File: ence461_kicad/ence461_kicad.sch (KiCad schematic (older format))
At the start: 52 parts

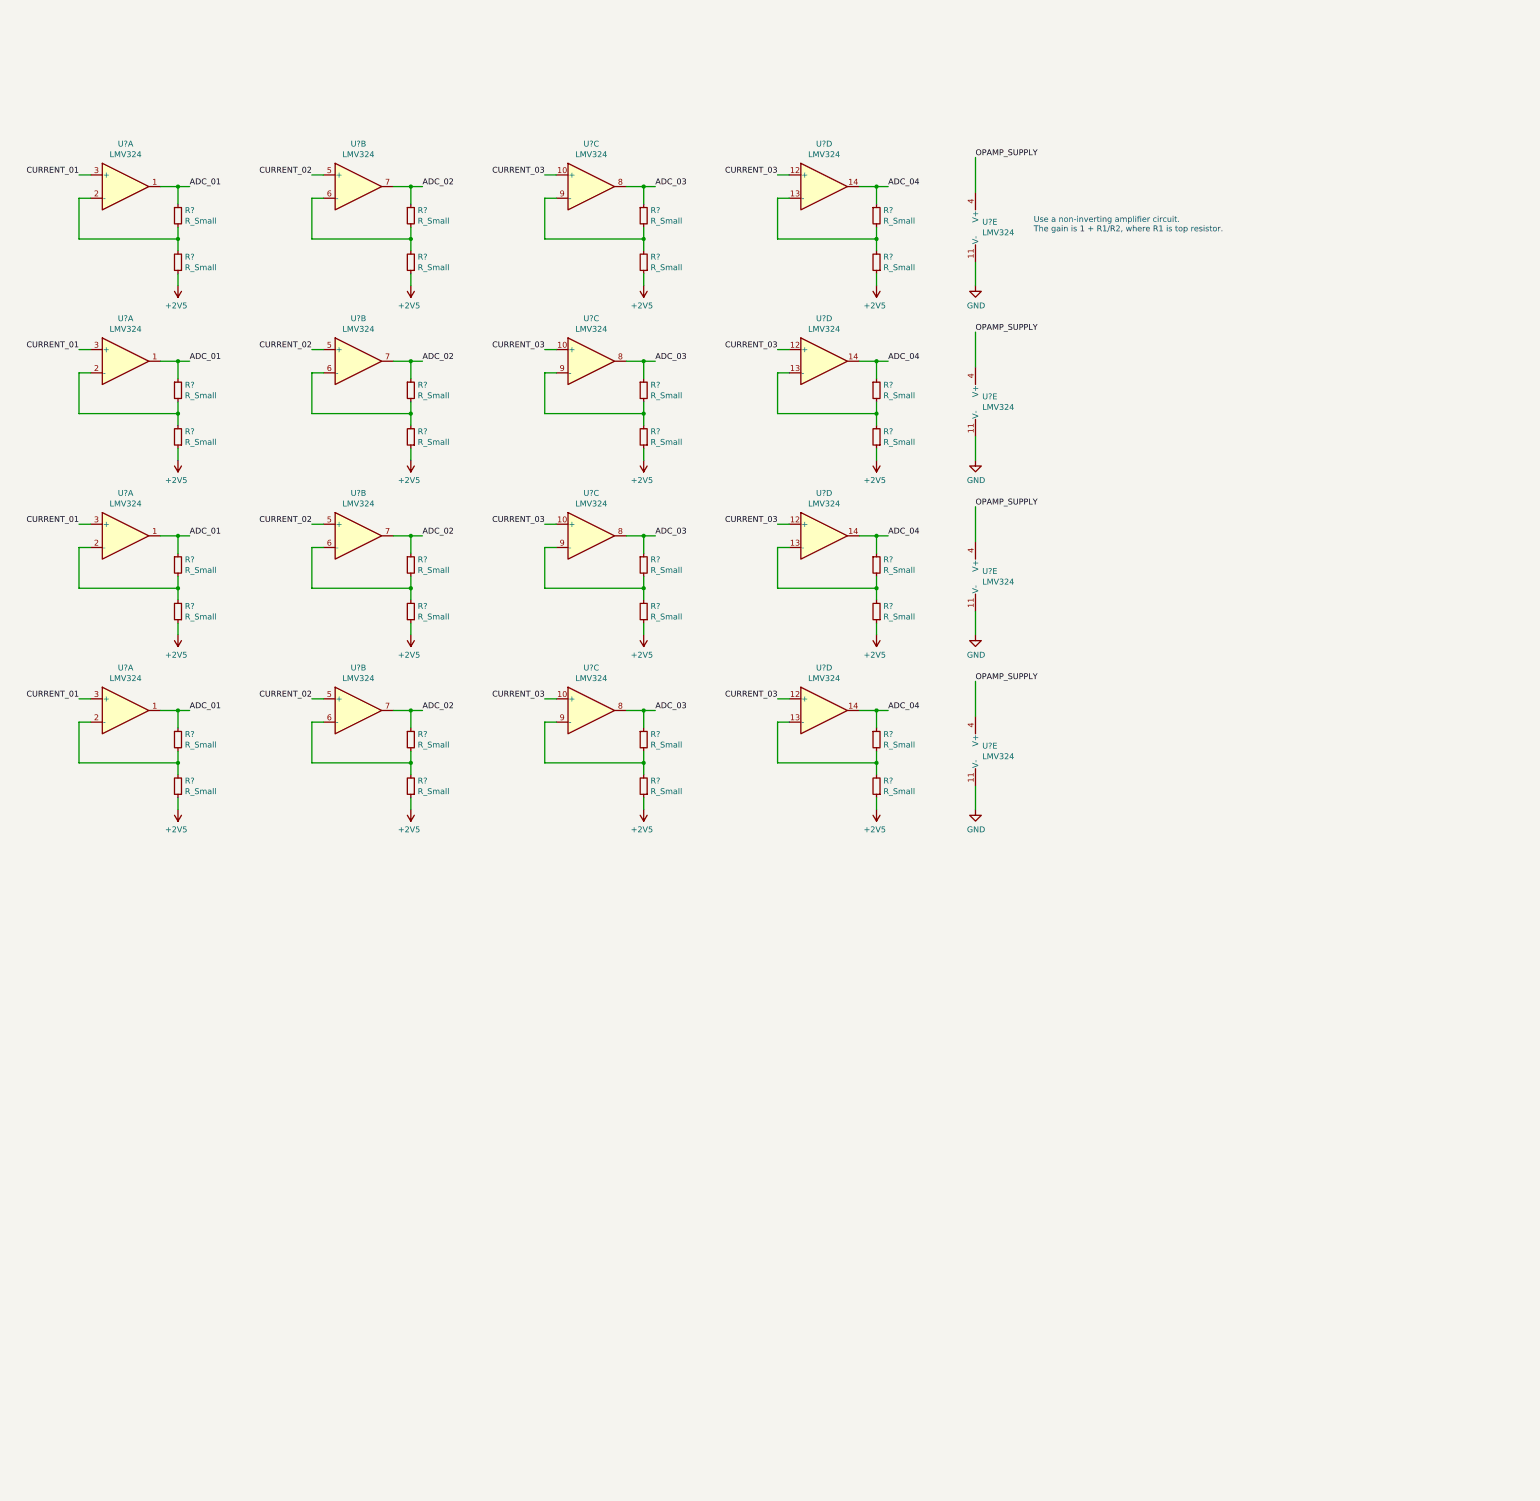
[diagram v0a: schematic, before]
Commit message: Added op amps to schematic. Specced an opamp for virtual gnd.
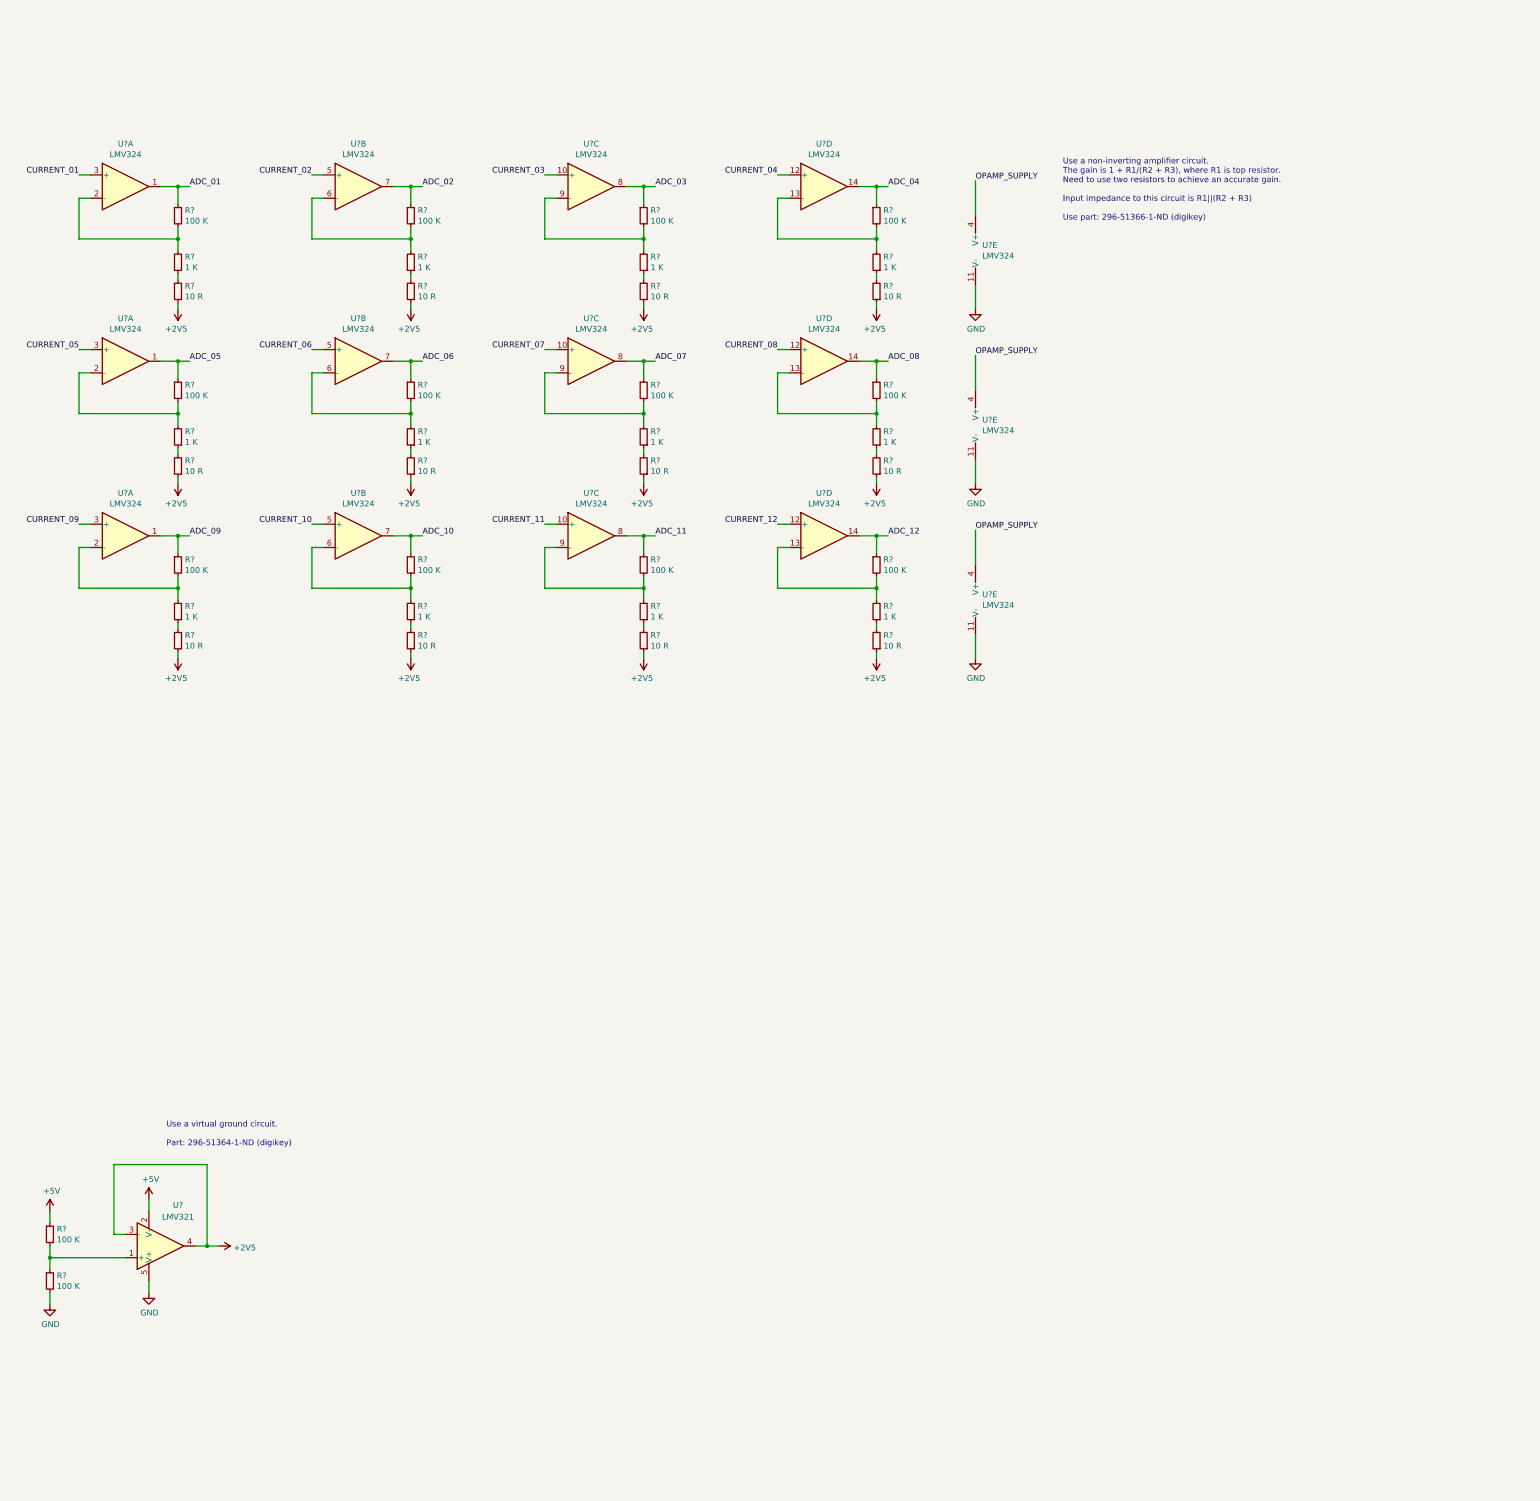
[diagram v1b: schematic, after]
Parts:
- removed R? (x24): R_Small, symbol Device:R_Small
- removed U? (x15): LMV324, symbol Amplifier_Operational:LMV324
- added R? (x12): 10 R, symbol Device:R_Small
- added R? (x10): 100 K, symbol Device:R_Small
- added R? (x8): 1 K, symbol Device:R_Small
- added U?: LMV321, symbol Amplifier_Operational:LMV321
- added U? (x10): LMV324, symbol Amplifier_Operational:LMV324
- R? (x4): value R_Small -> 100 K
- R? (x4): value R_Small -> 1 K
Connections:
- net +2V5: now also R?.1, R?.1, R?.1, R?.1, R?.1, R?.1, R?.1, R?.1, R?.1, R?.1, R?.1, R?.1, U?.3 (-), U?.4; no longer R?.1, R?.1, R?.1, R?.1
- net CURRENT_03: no longer U?.12 (+)
- net GND: now also R?.2, U?.11 (V-), U?.11 (V-), U?.5 (V+)
- net OPAMP_SUPPLY: now also U?.4 (V+), U?.4 (V+)
- new net: R?.1, R?.2 (x12)
- new net: R?.1, R?.2, U?.1 (+)
- new net: R?.2, R?.2, U?.2 (-) (x2)
- new net: R?.2, R?.2, U?.6 (-) (x2)
- new net: R?.2, R?.2, U?.9 (-) (x2)
- new net: R?.2, R?.2, U?.13 (-) (x2)
- new net +5V: R?.1, U?.2 (V-)
- new net ADC_05: R?.1, U?.1
- new net ADC_06: R?.1, U?.7
- new net ADC_07: R?.1, U?.8
- new net ADC_08: R?.1, U?.14
- new net ADC_09: R?.1, U?.1
- new net ADC_10: R?.1, U?.7
- new net ADC_11: R?.1, U?.8
- new net ADC_12: R?.1, U?.14
- new net CURRENT_04: U?.12 (+)
- new net CURRENT_05: U?.3 (+)
- new net CURRENT_06: U?.5 (+)
- new net CURRENT_07: U?.10 (+)
- new net CURRENT_08: U?.12 (+)
- new net CURRENT_09: U?.3 (+)
- new net CURRENT_10: U?.5 (+)
- new net CURRENT_11: U?.10 (+)
- new net CURRENT_12: U?.12 (+)
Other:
- note added: "Use a non-inverting amplifier circuit.\nThe gain is 1 + R1/(R2 + R3), where R1 is top resistor.\nNeed to use two resistors to achieve an accurate gain.\n\nInput impedance to this circuit is R1||(R2 + R3)\n\nUse part: 296-51366-1-ND (digikey)"
- note added: "Use a virtual ground circuit.\n\nPart: 296-51364-1-ND (digikey)"
- note removed: "Use a non-inverting amplifier circuit.\nThe gain is 1 + R1/R2, where R1 is top resistor."
- moved on the sheet: U?E

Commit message: Added hex inverter stuff
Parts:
- added U? (x14): 74HC14, symbol 74xx:74HC14
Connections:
- net labels added: ENABLE_01, ENABLE_02, ENABLE_03, ENABLE_04, ENABLE_05, ENABLE_06, ENABLE_07, ENABLE_08, ENABLE_09, ENABLE_10, ENABLE_11, ENABLE_12, SUPPLY_01, SUPPLY_02, SUPPLY_03, SUPPLY_04, SUPPLY_05, SUPPLY_06, SUPPLY_07, SUPPLY_08, SUPPLY_09, SUPPLY_10, SUPPLY_11, SUPPLY_12
- wire segments 151 -> 179

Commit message: Respecced the inverter
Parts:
- removed U? (x14): 74HC14, symbol 74xx:74HC14
- added U? (x4): 74HC3G14DP, Package_SO:VSSOP-8_2.3x2mm_P0.5mm, symbol ence461_symbol_library:74HC3G14DP
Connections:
- net labels removed: ENABLE_04, ENABLE_05, ENABLE_06, ENABLE_07, ENABLE_08, ENABLE_09, ENABLE_10, ENABLE_11, ENABLE_12, SUPPLY_04, SUPPLY_05, SUPPLY_06, SUPPLY_07, SUPPLY_08, SUPPLY_09, SUPPLY_10, SUPPLY_11, SUPPLY_12
- wire segments 179 -> 159
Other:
- note added: "Non-Inverting Amplifier Circuit"
- note added: "Op-Amp Enable Circuit"
- note added: "Virtual Ground Circuit"

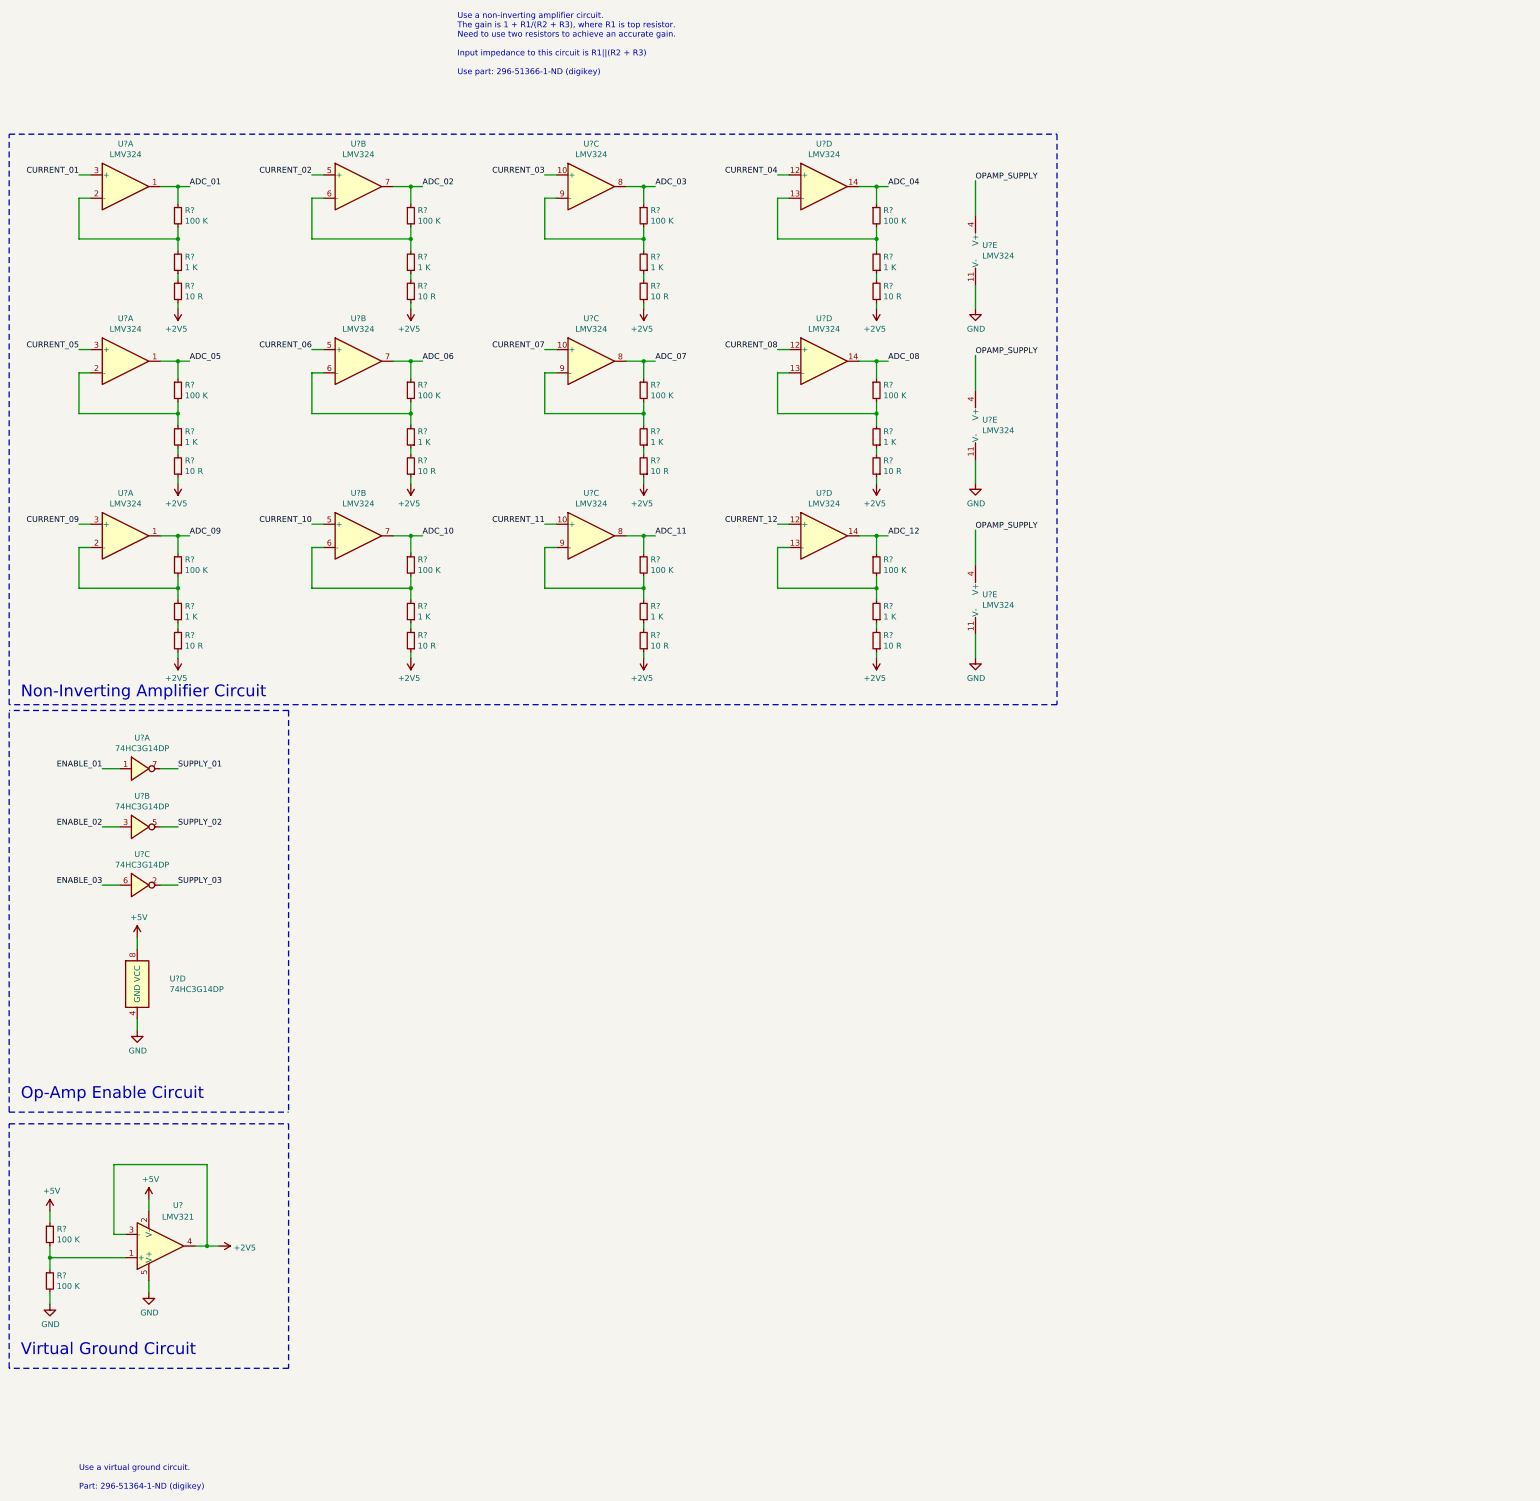
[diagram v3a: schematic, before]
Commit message: Added CAN transceiver symbol to schematic.
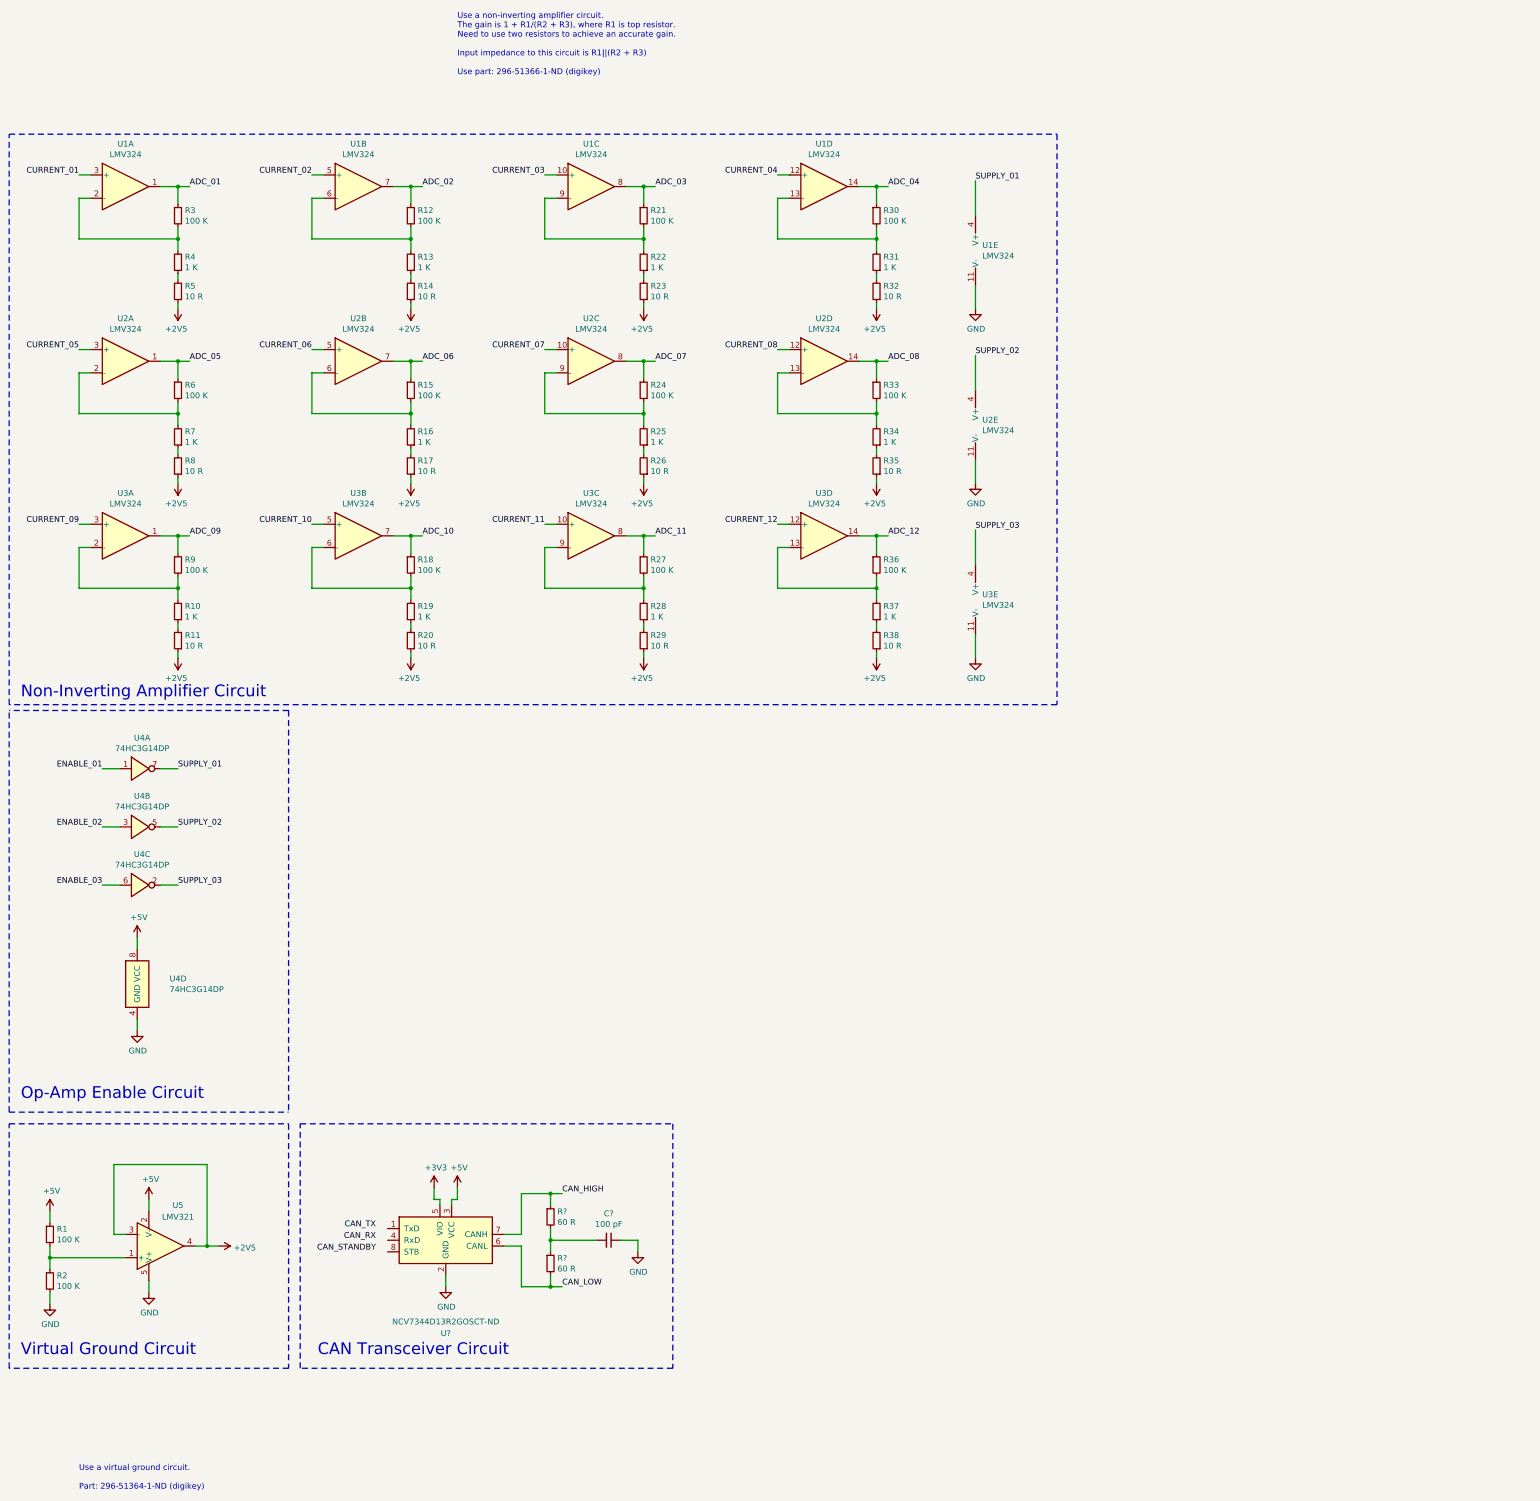
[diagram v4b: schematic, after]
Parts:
- added C?: 100 pF, symbol Device:C_Small
- added R? (x2): 60 R, symbol Device:R_Small
- added U?: NCV7344D13R2GOSCT-ND, Package_SO:SOIC-8_3.9x4.9mm_P1.27mm, symbol ence461_symbol_library:NCV7344D13R2GOSCT-ND
- gave numbers to parts that had none: 43
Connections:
- net +5V: now also U?.3 (VCC)
- net GND: now also C?.1, U?.2 (GND)
- net SUPPLY_01: now also U1.4 (V+)
- net SUPPLY_02: now also U2.4 (V+)
- net SUPPLY_03: now also U3.4 (V+)
- removed net OPAMP_SUPPLY: U1.4 (V+), U2.4 (V+), U3.4 (V+)
- new net: C?.2, R?.1, R?.2
- new net +3V3: U?.5 (VIO)
- new net CAN_HIGH: R?.1, U?.7 (CANH)
- new net CAN_LOW: R?.2, U?.6 (CANL)
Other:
- note added: "CAN Transceiver Circuit"
